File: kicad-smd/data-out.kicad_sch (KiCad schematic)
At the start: 49 parts, among them J1 Conn_01x16, U1 SGM6603-5.0, U2 LSF0204, U3 LSF0204, U4 LSF0204

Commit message: file updates
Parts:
- R11, R12, R13, R14, R15, R16, R17, R18, R19, R20: value 160 -> 200
- R30: value 160 -> 100
- RA1, RA10, RA11, RA12, RA2, RA3, RA4, RA5, RA6, RA7, RA8, RA9: value 180 -> 200
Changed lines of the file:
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@@
     (in_bom yes) (on_board yes)
     (property "Reference" "RA1" (id 0) (at 46.99 36.83 0))
-    (property "Value" "180" (id 1) (at 52.07 36.83 0))
+    (property "Value" "200" (id 1) (at 52.07 36.83 0))
     (property "Footprint" "FM4DD:R_Array_Convex_4x0603" (id 2) (at 50.038 56.896 0)
       (effects (font (size 1.27 1.27)) hide)
@@
     (in_bom yes) (on_board yes)
     (property "Reference" "RA10" (id 0) (at 127 107.95 0))
-    (property "Value" "180" (id 1) (at 132.08 107.95 0))
+    (property "Value" "200" (id 1) (at 132.08 107.95 0))
     (property "Footprint" "FM4DD:R_Array_Convex_4x0603" (id 2) (at 130.048 112.776 0)
       (effects (font (size 1.27 1.27)) hide)
@@
     (in_bom yes) (on_board yes)
     (property "Reference" "R19" (id 0) (at 45.72 172.72 90))
-    (property "Value" "160" (id 1) (at 53.34 175.26 90))
+    (property "Value" "200" (id 1) (at 53.34 175.26 90))
     (property "Footprint" "Resistor_SMD:R_0402_1005Metric" (id 2) (at 49.53 173.99 0)
       (effects (font (size 1.27 1.27)) hide)
@@
     (in_bom yes) (on_board yes)
     (property "Reference" "RA5" (id 0) (at 210.82 36.83 0))
-    (property "Value" "180" (id 1) (at 215.9 36.83 0))
+    (property "Value" "200" (id 1) (at 215.9 36.83 0))
     (property "Footprint" "FM4DD:R_Array_Convex_4x0603" (id 2) (at 213.868 56.896 0)
       (effects (font (size 1.27 1.27)) hide)
@@
     (in_bom yes) (on_board yes)
     (property "Reference" "R12" (id 0) (at 45.72 137.16 90))
-    (property "Value" "160" (id 1) (at 53.34 139.7 90))
+    (property "Value" "200" (id 1) (at 53.34 139.7 90))
     (property "Footprint" "Resistor_SMD:R_0402_1005Metric" (id 2) (at 49.53 138.43 0)
       (effects (font (size 1.27 1.27)) hide)
@@
     (in_bom yes) (on_board yes)
     (property "Reference" "RA9" (id 0) (at 127 80.01 0))
-    (property "Value" "180" (id 1) (at 132.08 80.01 0))
+    (property "Value" "200" (id 1) (at 132.08 80.01 0))
     (property "Footprint" "FM4DD:R_Array_Convex_4x0603" (id 2) (at 130.048 100.076 0)
       (effects (font (size 1.27 1.27)) hide)
@@
     (in_bom yes) (on_board yes)
     (property "Reference" "R17" (id 0) (at 45.72 162.56 90))
-    (property "Value" "160" (id 1) (at 53.34 165.1 90))
+    (property "Value" "200" (id 1) (at 53.34 165.1 90))
     (property "Footprint" "Resistor_SMD:R_0402_1005Metric" (id 2) (at 49.53 163.83 0)
       (effects (font (size 1.27 1.27)) hide)
@@
     (in_bom yes) (on_board yes)
     (property "Reference" "R15" (id 0) (at 45.72 152.4 90))
-    (property "Value" "160" (id 1) (at 53.34 154.94 90))
+    (property "Value" "200" (id 1) (at 53.34 154.94 90))
     (property "Footprint" "Resistor_SMD:R_0402_1005Metric" (id 2) (at 49.53 153.67 0)
       (effects (font (size 1.27 1.27)) hide)
@@
     (in_bom yes) (on_board yes)
     (property "Reference" "RA7" (id 0) (at 46.99 80.01 0))
-    (property "Value" "180" (id 1) (at 52.07 80.01 0))
+    (property "Value" "200" (id 1) (at 52.07 80.01 0))
     (property "Footprint" "FM4DD:R_Array_Convex_4x0603" (id 2) (at 50.038 100.076 0)
       (effects (font (size 1.27 1.27)) hide)
@@
     (in_bom yes) (on_board yes)
     (property "Reference" "RA4" (id 0) (at 127 64.77 0))
-    (property "Value" "180" (id 1) (at 132.08 64.77 0))
+    (property "Value" "200" (id 1) (at 132.08 64.77 0))
     (property "Footprint" "FM4DD:R_Array_Convex_4x0603" (id 2) (at 130.048 69.596 0)
       (effects (font (size 1.27 1.27)) hide)
@@
     (in_bom yes) (on_board yes)
     (property "Reference" "R11" (id 0) (at 45.72 132.08 90))
-    (property "Value" "160" (id 1) (at 53.34 134.62 90))
+    (property "Value" "200" (id 1) (at 53.34 134.62 90))
     (property "Footprint" "Resistor_SMD:R_0402_1005Metric" (id 2) (at 49.53 133.35 0)
       (effects (font (size 1.27 1.27)) hide)
@@
     (in_bom yes) (on_board yes)
     (property "Reference" "R16" (id 0) (at 45.72 157.48 90))
-    (property "Value" "160" (id 1) (at 53.34 160.02 90))
+    (property "Value" "200" (id 1) (at 53.34 160.02 90))
     (property "Footprint" "Resistor_SMD:R_0402_1005Metric" (id 2) (at 49.53 158.75 0)
       (effects (font (size 1.27 1.27)) hide)
@@
     (in_bom yes) (on_board yes)
     (property "Reference" "RA6" (id 0) (at 210.82 64.77 0))
-    (property "Value" "180" (id 1) (at 215.9 64.77 0))
+    (property "Value" "200" (id 1) (at 215.9 64.77 0))
     (property "Footprint" "FM4DD:R_Array_Convex_4x0603" (id 2) (at 213.868 69.596 0)
       (effects (font (size 1.27 1.27)) hide)
@@
     (in_bom yes) (on_board yes)
     (property "Reference" "R14" (id 0) (at 45.72 147.32 90))
-    (property "Value" "160" (id 1) (at 53.34 149.86 90))
+    (property "Value" "200" (id 1) (at 53.34 149.86 90))
     (property "Footprint" "Resistor_SMD:R_0402_1005Metric" (id 2) (at 49.53 148.59 0)
       (effects (font (size 1.27 1.27)) hide)
@@
     (in_bom yes) (on_board yes)
     (property "Reference" "R13" (id 0) (at 45.72 142.24 90))
-    (property "Value" "160" (id 1) (at 53.34 144.78 90))
+    (property "Value" "200" (id 1) (at 53.34 144.78 90))
     (property "Footprint" "Resistor_SMD:R_0402_1005Metric" (id 2) (at 49.53 143.51 0)
       (effects (font (size 1.27 1.27)) hide)
@@
     (in_bom yes) (on_board yes)
     (property "Reference" "RA11" (id 0) (at 210.82 80.01 0))
-    (property "Value" "180" (id 1) (at 215.9 80.01 0))
+    (property "Value" "200" (id 1) (at 215.9 80.01 0))
     (property "Footprint" "FM4DD:R_Array_Convex_4x0603" (id 2) (at 213.868 100.076 0)
       (effects (font (size 1.27 1.27)) hide)
@@
     (in_bom yes) (on_board yes)
     (property "Reference" "R30" (id 0) (at 152.4 134.62 90))
-    (property "Value" "160" (id 1) (at 160.02 137.16 90))
+    (property "Value" "100" (id 1) (at 160.02 137.16 90))
     (property "Footprint" "Resistor_THT:R_Axial_DIN0204_L3.6mm_D1.6mm_P5.08mm_Horizontal" (id 2) (at 156.21 135.89 0)
       (effects (font (size 1.27 1.27)) hide)
@@
     (in_bom yes) (on_board yes)
     (property "Reference" "RA3" (id 0) (at 127 36.83 0))
-    (property "Value" "180" (id 1) (at 132.08 36.83 0))
+    (property "Value" "200" (id 1) (at 132.08 36.83 0))
     (property "Footprint" "FM4DD:R_Array_Convex_4x0603" (id 2) (at 130.048 56.896 0)
       (effects (font (size 1.27 1.27)) hide)
@@
     (in_bom yes) (on_board yes)
     (property "Reference" "R18" (id 0) (at 45.72 167.64 90))
-    (property "Value" "160" (id 1) (at 53.34 170.18 90))
+    (property "Value" "200" (id 1) (at 53.34 170.18 90))
     (property "Footprint" "Resistor_SMD:R_0402_1005Metric" (id 2) (at 49.53 168.91 0)
       (effects (font (size 1.27 1.27)) hide)
@@
     (in_bom yes) (on_board yes)
     (property "Reference" "RA8" (id 0) (at 46.99 107.95 0))
-    (property "Value" "180" (id 1) (at 52.07 107.95 0))
+    (property "Value" "200" (id 1) (at 52.07 107.95 0))
     (property "Footprint" "FM4DD:R_Array_Convex_4x0603" (id 2) (at 50.038 112.776 0)
       (effects (font (size 1.27 1.27)) hide)
@@
     (in_bom yes) (on_board yes)
     (property "Reference" "RA2" (id 0) (at 46.99 64.77 0))
-    (property "Value" "180" (id 1) (at 52.07 64.77 0))
+    (property "Value" "200" (id 1) (at 52.07 64.77 0))
     (property "Footprint" "FM4DD:R_Array_Convex_4x0603" (id 2) (at 50.038 69.596 0)
       (effects (font (size 1.27 1.27)) hide)
@@
     (in_bom yes) (on_board yes)
     (property "Reference" "RA12" (id 0) (at 210.82 107.95 0))
-    (property "Value" "180" (id 1) (at 215.9 107.95 0))
+    (property "Value" "200" (id 1) (at 215.9 107.95 0))
     (property "Footprint" "FM4DD:R_Array_Convex_4x0603" (id 2) (at 213.868 112.776 0)
       (effects (font (size 1.27 1.27)) hide)
@@
     (in_bom yes) (on_board yes)
     (property "Reference" "R20" (id 0) (at 45.72 177.8 90))
-    (property "Value" "160" (id 1) (at 53.34 180.34 90))
+    (property "Value" "200" (id 1) (at 53.34 180.34 90))
     (property "Footprint" "Resistor_SMD:R_0402_1005Metric" (id 2) (at 49.53 179.07 0)
       (effects (font (size 1.27 1.27)) hide)

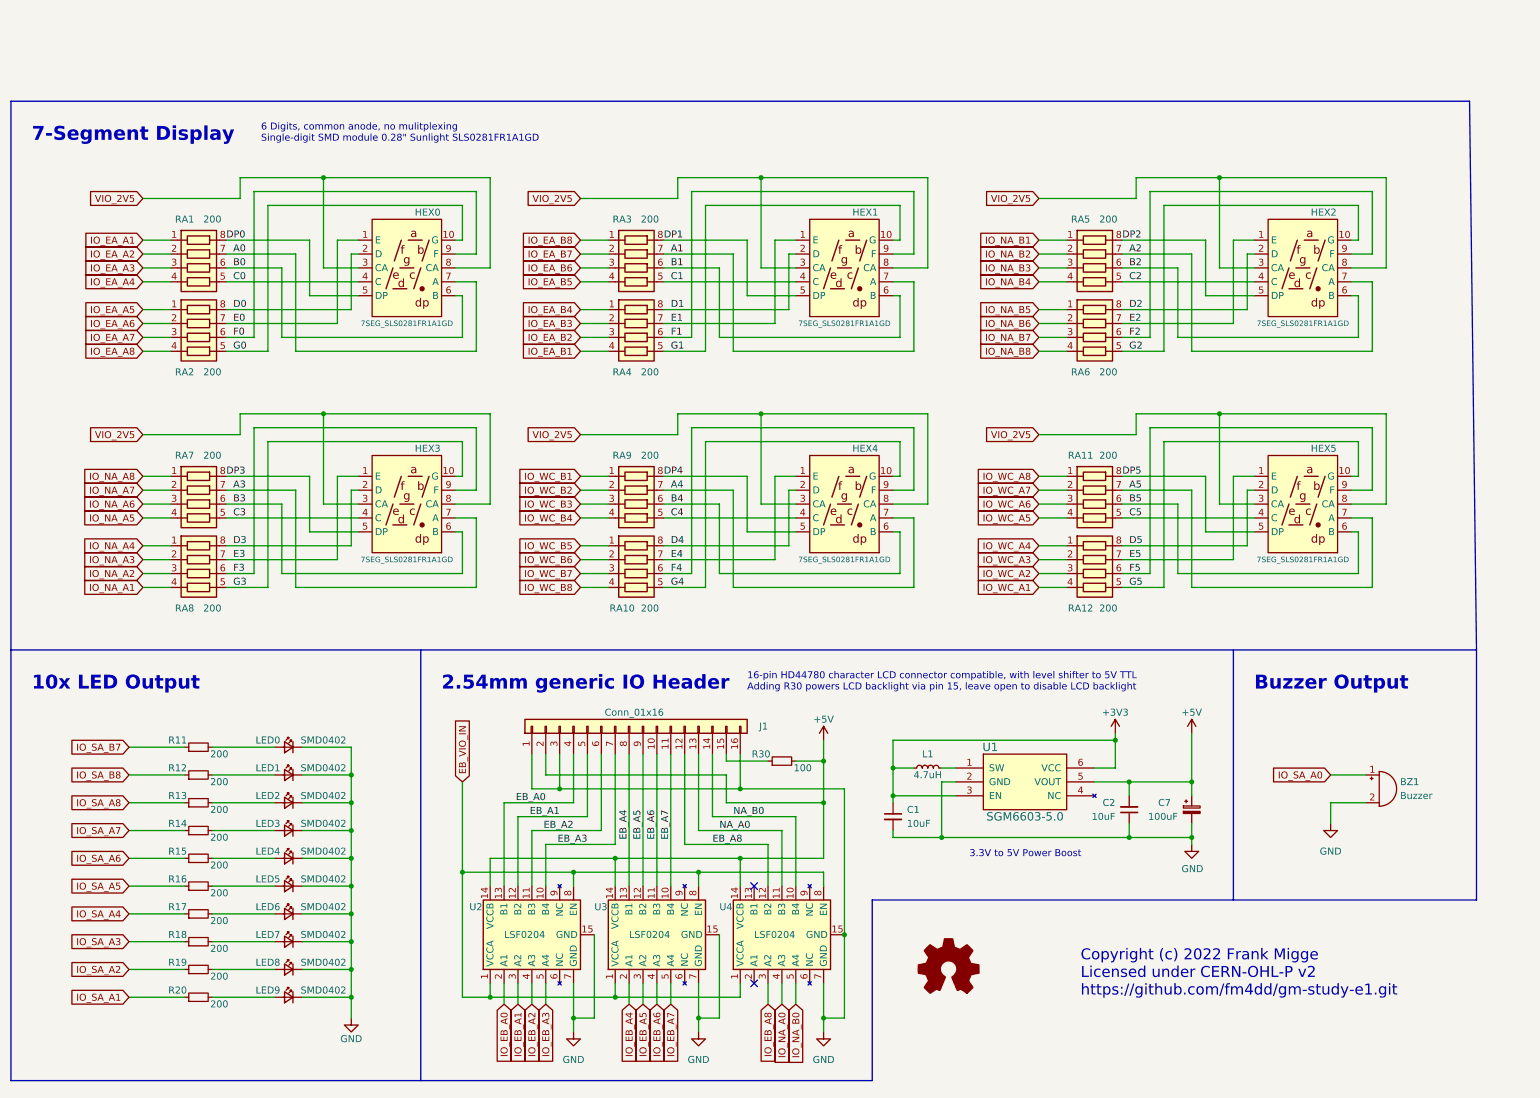
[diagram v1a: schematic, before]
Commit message: New SMB PCB v1.1 updates J1 level translation IC
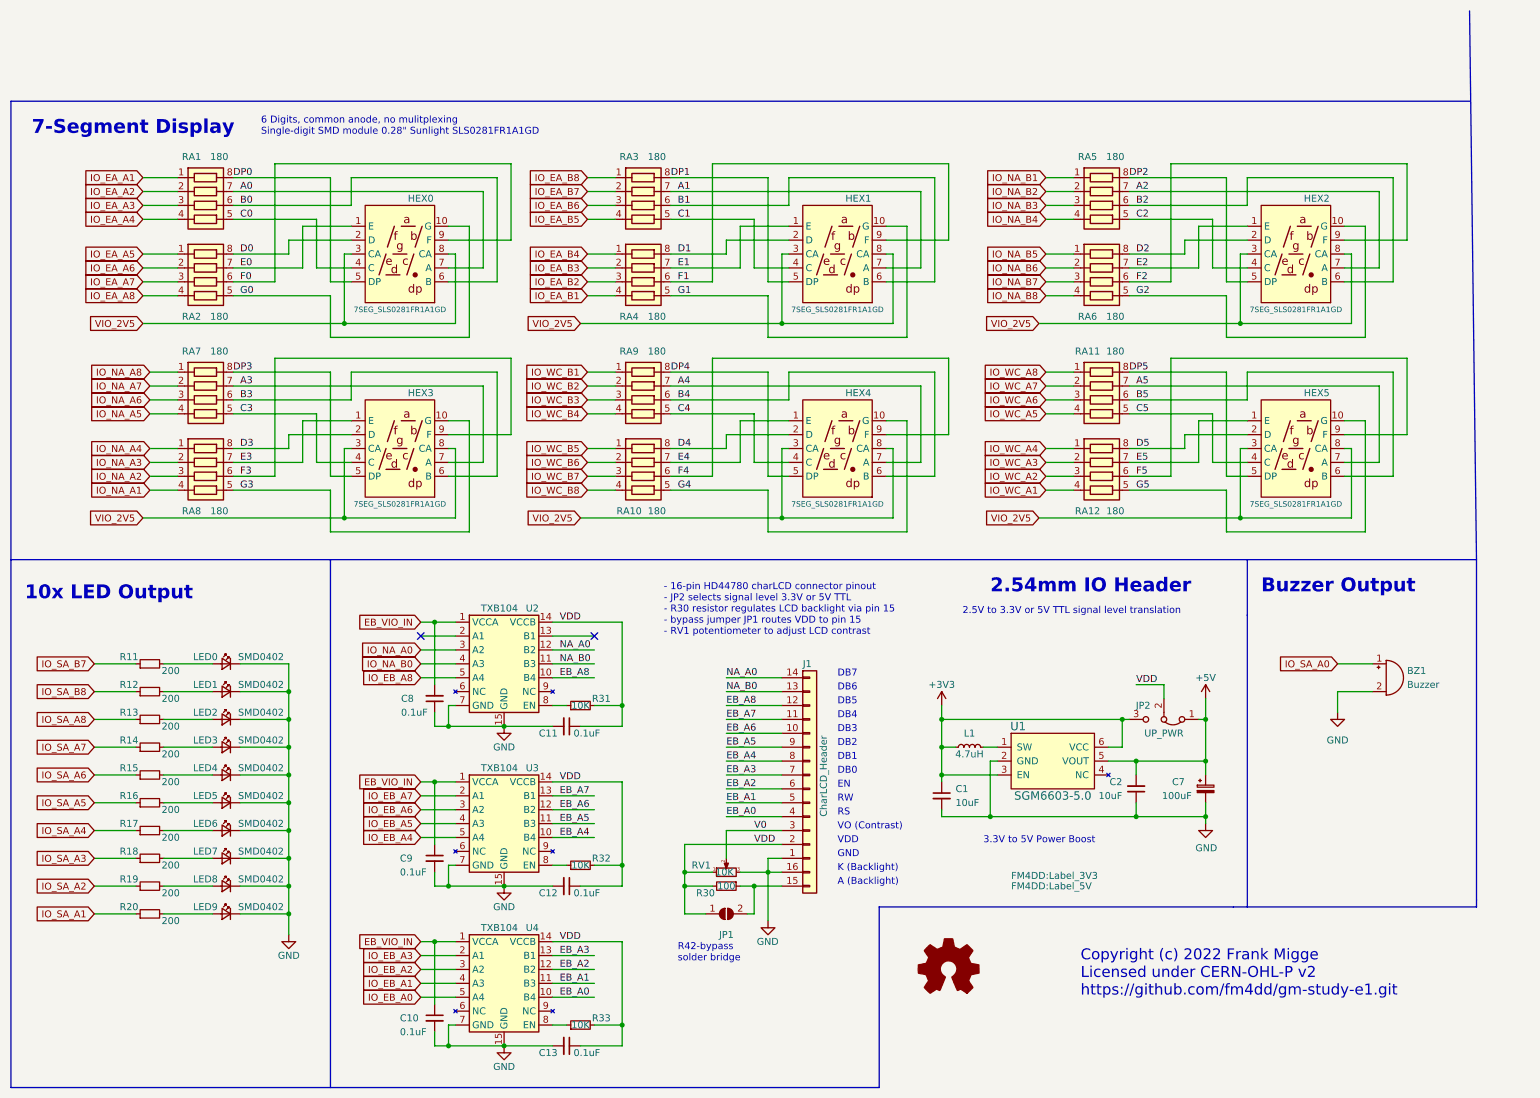
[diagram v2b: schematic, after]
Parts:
- removed J1: Conn_01x16, Connector_PinHeader_2.54mm:PinHeader_1x16_P2.54mm_Vertical, symbol Connector_Generic:Conn_01x16
- added C10, C11, C12, C13, C8, C9: 0.1uF, Capacitor_SMD:C_0402_1005Metric, symbol Device:C_Small
- added J1: CharLCD_Header, FM4DD:CharLCD Header, symbol FM4DD:CharLCD_Header
- added JP1: SolderJumper_2_Open, Jumper:SolderJumper-2_P1.3mm_Open_Pad1.0x1.5mm, symbol Jumper:SolderJumper_2_Open
- added JP2: UP_PWR, Connector_PinHeader_2.54mm:PinHeader_1x03_P2.54mm_Vertical, symbol Jumper:Jumper_3_Bridged12
- added LB5: Label_3V3, FM4DD:Label_3V3, symbol FM4DD:Label_3V3
- added LB6: Label_5V, FM4DD:Label_5V, symbol FM4DD:Label_5V
- added R31, R32, R33: 10K, Resistor_SMD:R_0402_1005Metric, symbol Device:R_Small
- added RV1: 10K, FM4DD:Potentiometer_Bourns_3362P_Vertical, symbol Device:R_Potentiometer_Small
- R30: footprint Resistor_THT:R_Axial_DIN0204_L3.6mm_D1.6mm_P5.08mm_Horizontal -> Resistor_SMD:R_0402_1005Metric
- RA1, RA10, RA11, RA12, RA2, RA3, RA4, RA5, RA6, RA7, RA8, RA9: value 200 -> 180
- U2, U3, U4: value LSF0204 -> TXB104
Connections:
- net +3V3: now also JP2.3 (B)
- net +5V: now also JP2.1 (A); no longer R30.2, U2.14 (VCCB), U3.14 (VCCB), U4.14 (VCCB)
- net EB_A0: now also U4.10 (B4), J1.4 (Pin_4); no longer U2.13 (B1)
- net EB_A1: now also U4.11 (B3), J1.5 (Pin_5); no longer U2.12 (B2)
- net EB_A2: now also U4.12 (B2), J1.6 (Pin_6); no longer U2.11 (B3)
- net EB_A3: now also U4.13 (B1), J1.7 (Pin_7); no longer U2.10 (B4)
- net EB_A4: now also U3.10 (B4), J1.8 (Pin_8); no longer U3.13 (B1)
- net EB_A5: now also U3.11 (B3), J1.9 (Pin_9); no longer U3.12 (B2)
- net EB_A6: now also U3.12 (B2), J1.10 (Pin_10); no longer U3.11 (B3)
- net EB_A7: now also U3.13 (B1), J1.11 (Pin_11); no longer U3.10 (B4)
- net EB_A8: now also U2.10 (B4), J1.12 (Pin_12); no longer U4.12 (B2)
- net EB_VIO_IN: now also C10.1, C8.2, C9.1; no longer U2.8 (EN), U3.8 (EN), U4.8 (EN)
- net GND: now also C10.2, C11.2, C12.2, C13.2, C8.1, C9.2, J1.1 (Pin_1), J1.16 (Pin_16), RV1.3
- net IO_EB_A0: now also U4.5 (A4); no longer U2.2 (A1)
- net IO_EB_A1: now also U4.4 (A3); no longer U2.3 (A2)
- net IO_EB_A2: now also U4.3 (A2); no longer U2.4 (A3)
- net IO_EB_A3: now also U4.2 (A1); no longer U2.5 (A4)
- net IO_EB_A4: now also U3.5 (A4); no longer U3.2 (A1)
- net IO_EB_A5: now also U3.4 (A3); no longer U3.3 (A2)
- net IO_EB_A6: now also U3.3 (A2); no longer U3.4 (A3)
- net IO_EB_A7: now also U3.2 (A1); no longer U3.5 (A4)
- net IO_EB_A8: now also U2.5 (A4); no longer U4.3 (A2)
- net IO_NA_A0: now also U2.3 (A2); no longer U4.4 (A3)
- net IO_NA_B0: now also U2.4 (A3); no longer U4.5 (A4)
- net NA_A0: now also U2.12 (B2), J1.14 (Pin_14); no longer U4.11 (B3)
- net NA_B0: now also U2.11 (B3), J1.13 (Pin_13); no longer U4.10 (B4)
- net at R30.1: now also J1.15 (Pin_15), JP1.2 (B)
- new net: R32.1, U3.8 (EN)
- new net: R31.1, U2.8 (EN)
- new net: R33.1, U4.8 (EN)
- new net V0: J1.3 (Pin_3), RV1.2
- new net VDD: C11.1, C12.1, C13.1, J1.2 (Pin_2), JP1.1 (A), JP2.2 (C), R30.2, R31.2, R32.2, R33.2, RV1.1, U2.14 (VCCB), U3.14 (VCCB), U4.14 (VCCB)
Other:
- note added: "- 16-pin HD44780 charLCD connector pinout - JP2 selects signal level 3.3V or 5V TTL - R30 resistor regulates LCD backlight via pin 15 - bypass jumper JP1 routes VDD to pin 15 - RV1 potentiometer to adjust LCD contrast"
- note added: "2.54mm IO Header"
- note added: "2.5V to 3.3V or 5V TTL signal level translation"
- note added: "A (Backlight)"
- note added: "DB0"
- note added: "DB1"
- note added: "DB2"
- note added: "DB3"
- note added: "DB4"
- note added: "DB5"
- note added: "DB6"
- note added: "DB7"
- note added: "EN"
- note added: "GND"
- note added: "K (Backlight)"
- note added: "R42-bypass solder bridge"
- note added: "RS"
- note added: "RW"
- note added: "VDD"
- note added: "VO (Contrast)"
- note removed: "16-pin HD44780 character LCD connector compatible, with level shifter to 5V TTL Adding R30 powers LCD backlight via pin 15, leave open to disable LCD backlight"
- note removed: "2.54mm generic IO Header"
- moved on the sheet: BZ1, LED0, LED1, LED2, LED3, LED4, LED5, LED6, LED7, LED8, LED9, R11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
